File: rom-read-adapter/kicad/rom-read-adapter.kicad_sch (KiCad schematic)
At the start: 0 parts

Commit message: WIP kicad-lib RRA: Add jumper to schematic, header pin to library
- Rename Header Pin to Jumper 1
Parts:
- added J1: ZIF-48, symbol 0cjs-hwdev:ZIF48
- added JP11, JPA13: Header_Pin, symbol 0cjs-hwdev:Header_Pin
- added JP12, JP13, JP14, JP15, JP16, JP17, JP18, JP19, JP20, JP21, JP22, JP23, JP24: Jumper_2_Open, symbol Jumper:Jumper_2_Open
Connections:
- new net: J1., J1.28
- new net: J1.11, JP11.2 (B)
- new net: J1.12, JP12.2 (B)
- new net: J1.13, JP13.2 (B)
- new net: J1.14, JP14.2 (B)
- new net: J1.15, JP15.2 (B)
- new net: J1.16, JP16.2 (B)
- new net: J1.17, JP17.2 (B)
- new net: J1.18, JP18.2 (B)
- new net: J1.19, JP19.2 (B)
- new net: J1.20, JP20.2 (B)
- new net: J1.21, JP21.2 (B)
- new net: J1.22, JP22.2 (B)
- new net: J1.23, JP23.2 (B)
- new net: J1.24, JP24.2 (B)
- new net A13: JPA13.2 (B)
- new net D0: JP21.1 (A)
- new net D1: JP22.1 (A)
- new net D2: JP23.1 (A)
- new net GND: JP24.1 (A)

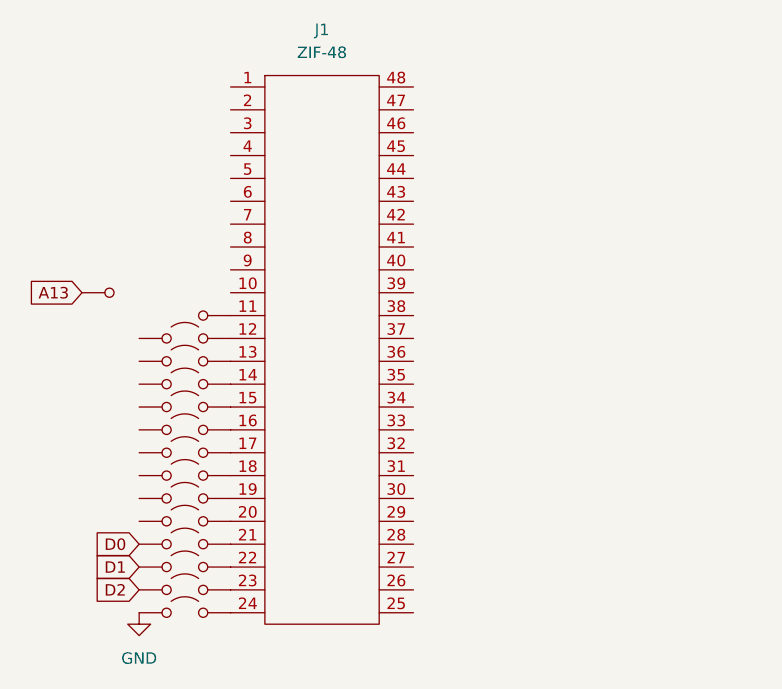
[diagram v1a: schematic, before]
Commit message: WIP kicad RRA: Added Jumpers, header pins, power symbols
- need to add CS and resize header pins
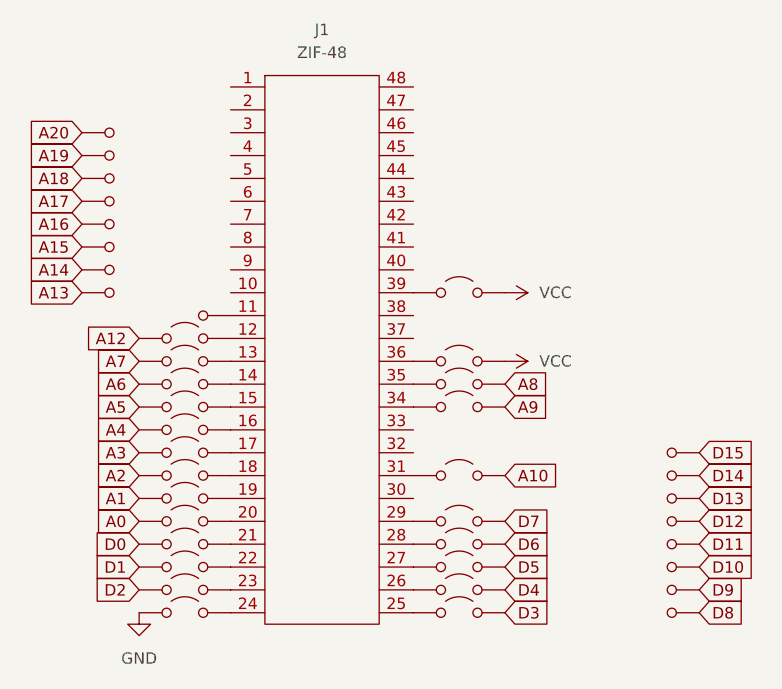
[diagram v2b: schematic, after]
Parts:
- added JP25, JP26, JP27, JP28, JP29, JP31, JP34, JP35, JP36, JP39: Jumper_2_Open, symbol Jumper:Jumper_2_Open
- added JPA1, JPA10, JPA11, JPA12, JPA14, JPA15, JPA16, JPA2, JPA3, JPA4, JPA5, JPA6, JPA7, JPA8, JPA9: Header_Pin, symbol 0cjs-hwdev:Header_Pin
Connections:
- net at J1., J1.28: now also JP28.1 (A)
- net at J1.25: now also JP25.1 (A)
- net at J1.26: now also JP26.1 (A)
- net at J1.27: now also JP27.1 (A)
- net at J1.29: now also JP29.1 (A)
- net at J1.31: now also JP31.1 (A)
- net at J1.34: now also JP34.1 (A)
- net at J1.35: now also JP35.1 (A)
- net at J1.36: now also JP36.1 (A)
- net at J1.39: now also JP39.1 (A)
- net A7: now reaches JP13.1 (A)
- net A4: now reaches JP16.1 (A)
- net A1: now reaches JP19.1 (A)
- net A2: now reaches JP18.1 (A)
- net A6: now reaches JP14.1 (A)
- net A12: now reaches JP12.1 (A)
- net A3: now reaches JP17.1 (A)
- net A0: now reaches JP20.1 (A)
- net A5: now reaches JP15.1 (A)
- new net A10: JP31.2 (B)
- new net A14: JPA1.2 (B)
- new net A15: JPA2.2 (B)
- new net A16: JPA3.2 (B)
- new net A17: JPA4.2 (B)
- new net A18: JPA5.2 (B)
- new net A19: JPA6.2 (B)
- new net A20: JPA7.2 (B)
- new net A8: JP35.2 (B)
- new net A9: JP34.2 (B)
- new net D10: JPA10.2 (B)
- new net D11: JPA11.2 (B)
- new net D12: JPA12.2 (B)
- new net D13: JPA14.2 (B)
- new net D14: JPA15.2 (B)
- new net D15: JPA16.2 (B)
- new net D3: JP25.2 (B)
- new net D4: JP26.2 (B)
- new net D5: JP27.2 (B)
- new net D6: JP28.2 (B)
- new net D7: JP29.2 (B)
- new net D8: JPA8.2 (B)
- new net D9: JPA9.2 (B)
- new net VCC: JP36.2 (B), JP39.2 (B)

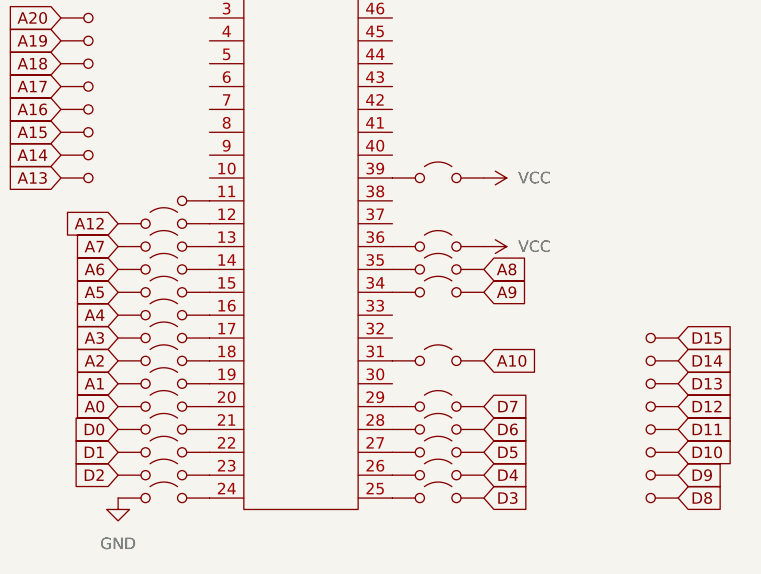
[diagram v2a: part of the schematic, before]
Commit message: kicad RRA sch: Add pin numbers for DIP 24 and 28
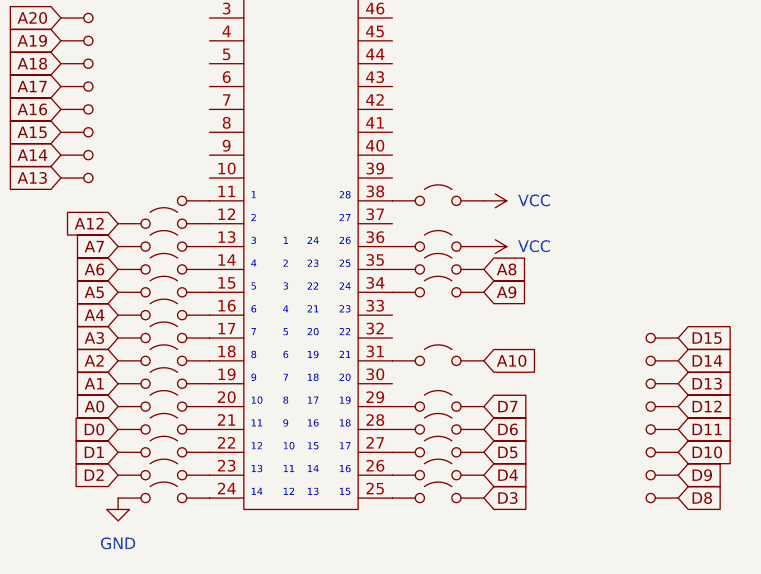
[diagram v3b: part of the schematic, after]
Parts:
- removed JP39: Jumper_2_Open, symbol Jumper:Jumper_2_Open
- added JP38: Jumper_2_Open, symbol Jumper:Jumper_2_Open
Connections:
- net VCC: now also JP38.2 (B)
- net at J1.38: now also JP38.1 (A)
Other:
- note added: "1 2 3 4 5 6 7 8 9 10 11 12"
- note added: "1 2 3 4 5 6 7 8 9 10 11 12 13 14"
- note added: "24 23 22 21 20 19 18 17 16 15 14 13"
- note added: "28 27 26 25 24 23 22 21 20 19 18 17 16 15"
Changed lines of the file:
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@@
 	(generator_version "9.0")
 	(paper "A4")
+	(text "28\n\n27\n\n26\n\n25\n\n24\n\n23\n\n22\n\n21\n\n20\n\n19\n\n18\n\n17\n\n16\n\n15"
+		(exclude_from_sim no)
+		(at 144.018 123.19 0)
+		(effects
+			(font
+				(size 0.7874 0.7874)
+			)
+			(justify right bottom)
+		)
+	)
+	(text "1\n\n2\n\n3\n\n4\n\n5\n\n6\n\n7\n\n8\n\n9\n\n10\n\n11\n\n12"
+		(exclude_from_sim no)
+		(at 136.398 123.19 0)
+		(effects
+			(font
+				(size 0.7874 0.7874)
+			)
+			(justify left bottom)
+		)
+	)
+	(text "24\n\n23\n\n22\n\n21\n\n20\n\n19\n\n18\n\n17\n\n16\n\n15\n\n14\n\n13"
+		(exclude_from_sim no)
+		(at 140.462 123.19 0)
+		(effects
+			(font
+				(size 0.7874 0.7874)
+			)
+			(justify right bottom)
+		)
+	)
+	(text "1\n\n2\n\n3\n\n4\n\n5\n\n6\n\n7\n\n8\n\n9\n\n10\n\n11\n\n12\n\n13\n\n14"
+		(exclude_from_sim no)
+		(at 132.842 123.19 0)
+		(effects
+			(font
+				(size 0.7874 0.7874)
+			)
+			(justify left bottom)
+		)
+	)
 	(global_label "A16"
 		(shape input)
@@
 	(symbol
 		(lib_id "Jumper:Jumper_2_Open")
-		(at 123.19 115.57 0)
+		(at 153.67 90.17 0)
 		(unit 1)
 		(exclude_from_sim no)
@@
 		(dnp no)
 		(fields_autoplaced yes)
-		(property "Reference" "JP21"
-			(at 123.19 109.22 0)
+		(property "Reference" "JP38"
+			(at 153.67 83.82 0)
 			(effects
 				(font
@@
 		)
 		(property "Value" "Jumper_2_Open"
-			(at 123.19 111.76 0)
+			(at 153.67 86.36 0)
 			(effects
 				(font
@@
 		)
 		(property "Footprint" ""
-			(at 123.19 115.57 0)
+			(at 153.67 90.17 0)
 			(effects
 				(font
@@
 		)
 		(property "Datasheet" "~"
-			(at 123.19 115.57 0)
+			(at 153.67 90.17 0)
 			(effects
 				(font
@@
 		)
 		(property "Description" "Jumper, 2-pole, open"
-			(at 123.19 115.57 0)
+			(at 153.67 90.17 0)
 			(effects
 				(font
@@
 			(project "rom-read-adapter"
 				(path "/65bf6d13-0c24-4e8f-8a57-e3ae2776eac6"
-					(reference "JP21")
+					(reference "JP38")
 					(unit 1)
 				)
@@
 	(symbol
 		(lib_id "Jumper:Jumper_2_Open")
-		(at 123.19 97.79 0)
+		(at 123.19 115.57 0)
 		(unit 1)
 		(exclude_from_sim no)
@@
 		(dnp no)
 		(fields_autoplaced yes)
-		(property "Reference" "JP14"
-			(at 123.19 91.44 0)
+		(property "Reference" "JP21"
+			(at 123.19 109.22 0)
 			(effects
 				(font
@@
 		)
 		(property "Value" "Jumper_2_Open"
-			(at 123.19 93.98 0)
+			(at 123.19 111.76 0)
 			(effects
 				(font
@@
 		)
 		(property "Footprint" ""
-			(at 123.19 97.79 0)
+			(at 123.19 115.57 0)
 			(effects
 				(font
@@
 		)
 		(property "Datasheet" "~"
-			(at 123.19 97.79 0)
+			(at 123.19 115.57 0)
 			(effects
 				(font
@@
 		)
 		(property "Description" "Jumper, 2-pole, open"
-			(at 123.19 97.79 0)
+			(at 123.19 115.57 0)
 			(effects
 				(font
@@
 			(project "rom-read-adapter"
 				(path "/65bf6d13-0c24-4e8f-8a57-e3ae2776eac6"
-					(reference "JP14")
+					(reference "JP21")
 					(unit 1)
 				)
@@
 	(symbol
 		(lib_id "Jumper:Jumper_2_Open")
-		(at 153.67 118.11 0)
+		(at 123.19 97.79 0)
 		(unit 1)
 		(exclude_from_sim no)
@@
 		(dnp no)
 		(fields_autoplaced yes)
-		(property "Reference" "JP27"
-			(at 153.67 111.76 0)
+		(property "Reference" "JP14"
+			(at 123.19 91.44 0)
 			(effects
 				(font
@@
 		)
 		(property "Value" "Jumper_2_Open"
-			(at 153.67 114.3 0)
+			(at 123.19 93.98 0)
 			(effects
 				(font
@@
 		)
 		(property "Footprint" ""
-			(at 153.67 118.11 0)
+			(at 123.19 97.79 0)
 			(effects
 				(font
@@
 		)
 		(property "Datasheet" "~"
-			(at 153.67 118.11 0)
+			(at 123.19 97.79 0)
 			(effects
 				(font
@@
 		)
 		(property "Description" "Jumper, 2-pole, open"
-			(at 153.67 118.11 0)
+			(at 123.19 97.79 0)
 			(effects
 				(font
@@
 			(project "rom-read-adapter"
 				(path "/65bf6d13-0c24-4e8f-8a57-e3ae2776eac6"
-					(reference "JP27")
+					(reference "JP14")
 					(unit 1)
 				)
@@
 	(symbol
 		(lib_id "Jumper:Jumper_2_Open")
-		(at 123.19 92.71 0)
+		(at 153.67 118.11 0)
 		(unit 1)
 		(exclude_from_sim no)
@@
 		(dnp no)
 		(fields_autoplaced yes)
-		(property "Reference" "JP12"
-			(at 123.19 86.36 0)
+		(property "Reference" "JP27"
+			(at 153.67 111.76 0)
 			(effects
 				(font
@@
 		)
 		(property "Value" "Jumper_2_Open"
-			(at 123.19 88.9 0)
+			(at 153.67 114.3 0)
 			(effects
 				(font
@@
 		)
 		(property "Footprint" ""
-			(at 123.19 92.71 0)
+			(at 153.67 118.11 0)
 			(effects
 				(font
@@
 		)
 		(property "Datasheet" "~"
-			(at 123.19 92.71 0)
+			(at 153.67 118.11 0)
 			(effects
 				(font
@@
 		)
 		(property "Description" "Jumper, 2-pole, open"
-			(at 123.19 92.71 0)
+			(at 153.67 118.11 0)
 			(effects
 				(font
@@
 			(project "rom-read-adapter"
 				(path "/65bf6d13-0c24-4e8f-8a57-e3ae2776eac6"
-					(reference "JP12")
+					(reference "JP27")
 					(unit 1)
 				)
@@
 	(symbol
 		(lib_id "Jumper:Jumper_2_Open")
-		(at 153.67 97.79 0)
+		(at 123.19 92.71 0)
 		(unit 1)
 		(exclude_from_sim no)
@@
 		(dnp no)
 		(fields_autoplaced yes)
-		(property "Reference" "JP35"
-			(at 153.67 91.44 0)
+		(property "Reference" "JP12"
+			(at 123.19 86.36 0)
 			(effects
 				(font
@@
 		)
 		(property "Value" "Jumper_2_Open"
-			(at 153.67 93.98 0)
+			(at 123.19 88.9 0)
 			(effects
 				(font
@@
 		)
 		(property "Footprint" ""
-			(at 153.67 97.79 0)
+			(at 123.19 92.71 0)
 			(effects
 				(font
@@
 		)
 		(property "Datasheet" "~"
-			(at 153.67 97.79 0)
+			(at 123.19 92.71 0)
 			(effects
 				(font
@@
 		)
 		(property "Description" "Jumper, 2-pole, open"
-			(at 153.67 97.79 0)
+			(at 123.19 92.71 0)
 			(effects
 				(font
@@
 			(project "rom-read-adapter"
 				(path "/65bf6d13-0c24-4e8f-8a57-e3ae2776eac6"
-					(reference "JP35")
+					(reference "JP12")
 					(unit 1)
 				)
@@
 	(symbol
 		(lib_id "Jumper:Jumper_2_Open")
-		(at 153.67 87.63 0)
+		(at 153.67 97.79 0)
 		(unit 1)
 		(exclude_from_sim no)
@@
 		(dnp no)
 		(fields_autoplaced yes)
-		(property "Reference" "JP39"
-			(at 153.67 81.28 0)
+		(property "Reference" "JP35"
+			(at 153.67 91.44 0)
 			(effects
 				(font
@@
 		)
 		(property "Value" "Jumper_2_Open"
-			(at 153.67 83.82 0)
+			(at 153.67 93.98 0)
 			(effects
 				(font
@@
 		)
 		(property "Footprint" ""
-			(at 153.67 87.63 0)
+			(at 153.67 97.79 0)
 			(effects
 				(font
@@
 		)
 		(property "Datasheet" "~"
-			(at 153.67 87.63 0)
+			(at 153.67 97.79 0)
 			(effects
 				(font
@@
 		)
 		(property "Description" "Jumper, 2-pole, open"
-			(at 153.67 87.63 0)
+			(at 153.67 97.79 0)
 			(effects
 				(font
@@
 			(project "rom-read-adapter"
 				(path "/65bf6d13-0c24-4e8f-8a57-e3ae2776eac6"
-					(reference "JP39")
+					(reference "JP35")
 					(unit 1)
 				)
@@
 	(symbol
 		(lib_id "power:VCC")
-		(at 158.75 87.63 270)
+		(at 158.75 90.17 270)
 		(unit 1)
 		(exclude_from_sim no)
@@
 		(fields_autoplaced yes)
 		(property "Reference" "#PWR39"
-			(at 154.94 87.63 0)
+			(at 154.94 90.17 0)
 			(effects
 				(font
@@
 		)
 		(property "Value" "VCC"
-			(at 162.56 87.6299 90)
+			(at 162.56 90.1699 90)
 			(effects
 				(font
@@
 		)
 		(property "Footprint" ""
-			(at 158.75 87.63 0)
+			(at 158.75 90.17 0)
 			(effects
 				(font
@@
 		)
 		(property "Datasheet" ""
-			(at 158.75 87.63 0)
+			(at 158.75 90.17 0)
 			(effects
 				(font
@@
 		)
 		(property "Description" "Power symbol creates a global label with name \"VCC\""
-			(at 158.75 87.63 0)
+			(at 158.75 90.17 0)
 			(effects
 				(font

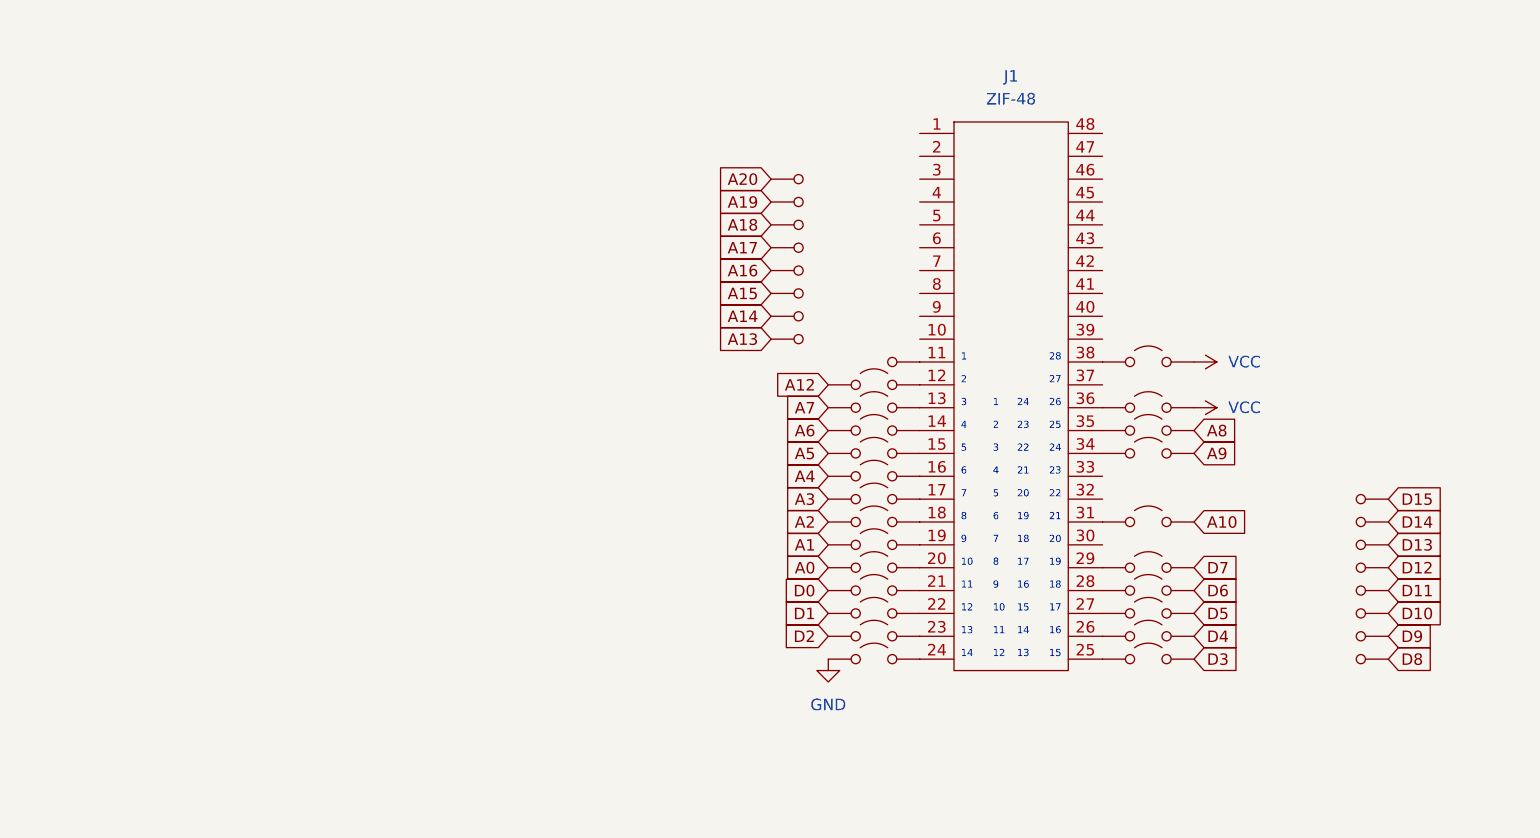
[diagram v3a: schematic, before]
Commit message: kicad RRA: Need to replace all jumpers with PIN headers
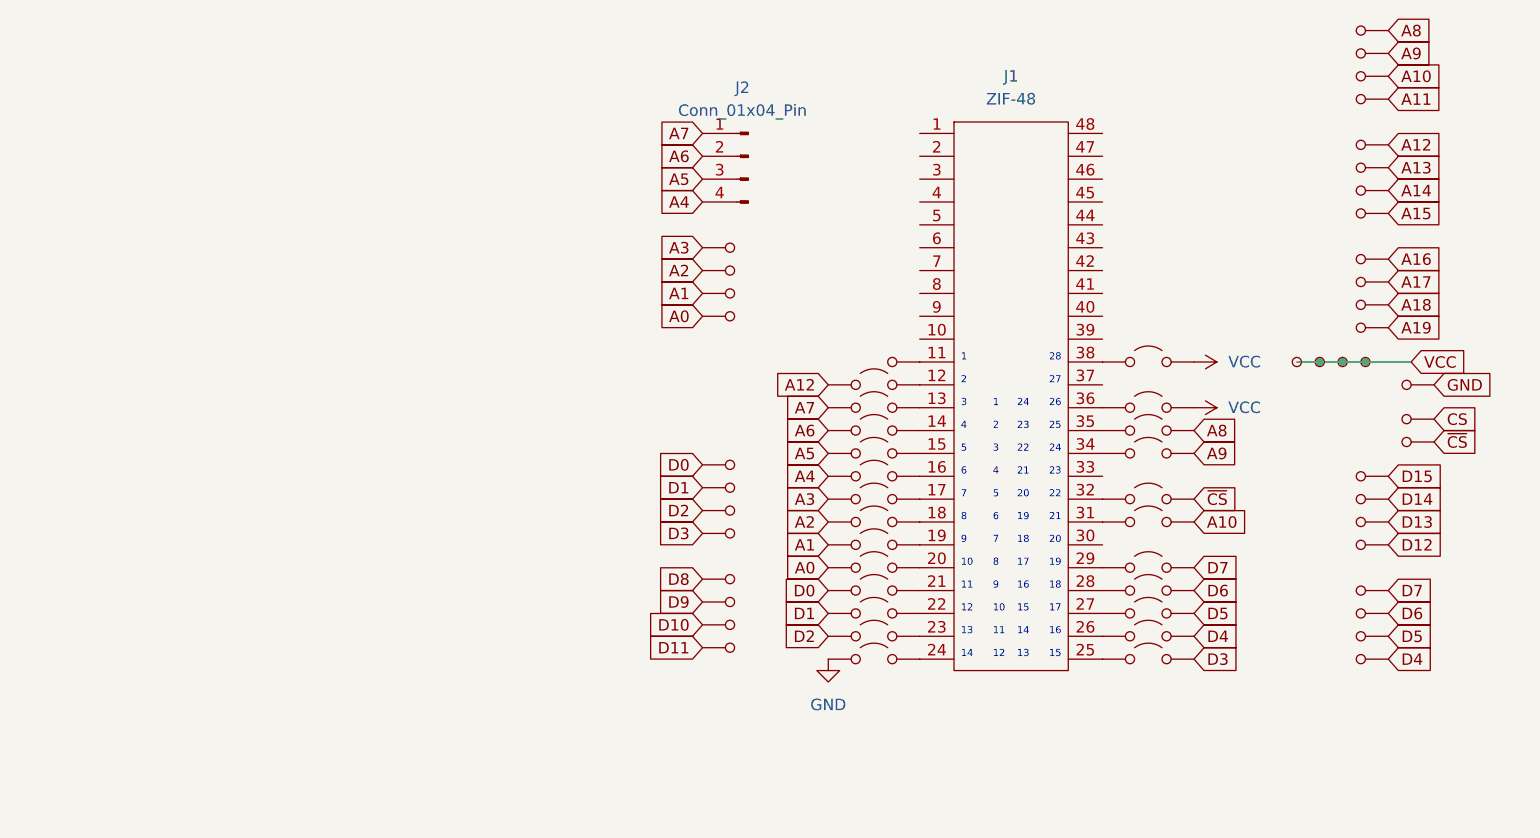
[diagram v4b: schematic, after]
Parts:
- added J2: Conn_01x04_Pin, symbol Connector:Conn_01x04_Pin
- added JP32: Jumper_2_Open, symbol Jumper:Jumper_2_Open
- added JPA17, JPA18, JPA19, JPA20, JPA25, JPA26, JPA27, JPA28, JPA29, JPA30, JPA31, JPA32, JPA33, JPA34, JPA35, JPA36, JPA37, JPA38, JPA39, JPA40, JPA41, JPA42, JPA43: Header_Pin, symbol 0cjs-hwdev:Header_Pin
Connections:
- net A20 is gone; now on net A12: JPA7.2 (B)
- net A0: now also JPA28.2 (B)
- net A1: now also JPA27.2 (B)
- net A10: now also JPA18.2 (B)
- net A2: now also JPA26.2 (B)
- net A3: now also JPA25.2 (B)
- net A4: now also J2.4 (Pin_4)
- net A5: now also J2.3 (Pin_3)
- net A6: now also J2.2 (Pin_2)
- net A7: now also J2.1 (Pin_1)
- net A8: now also JPA20.2 (B)
- net A9: now also JPA19.2 (B)
- net D0: now also JPA33.2 (B)
- net D1: now also JPA34.2 (B)
- net D10: now also JPA31.2 (B); no longer JPA10.2 (B)
- net D11: now also JPA32.2 (B); no longer JPA11.2 (B)
- net D2: now also JPA35.2 (B)
- net D3: now also JPA36.2 (B)
- net D4: now also JPA8.2 (B)
- net D5: now also JPA9.2 (B)
- net D6: now also JPA10.2 (B)
- net D7: now also JPA11.2 (B)
- net D8: now also JPA29.2 (B); no longer JPA8.2 (B)
- net D9: now also JPA30.2 (B); no longer JPA9.2 (B)
- net GND: now also JPA38.2 (B)
- net VCC: now also JPA37.2 (B), JPA41.2 (B), JPA42.2 (B), JPA43.2 (B)
- net at J1.32: now also JP32.1 (A)
- new net A11: JPA17.2 (B)
- new net CS: JPA39.2 (B)
- new net ~{CS}: JP32.2 (B), JPA40.2 (B)
